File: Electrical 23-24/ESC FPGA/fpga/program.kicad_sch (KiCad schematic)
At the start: 7 parts, among them SW2 SW_Push, U1 XC6SLX4-TQG144

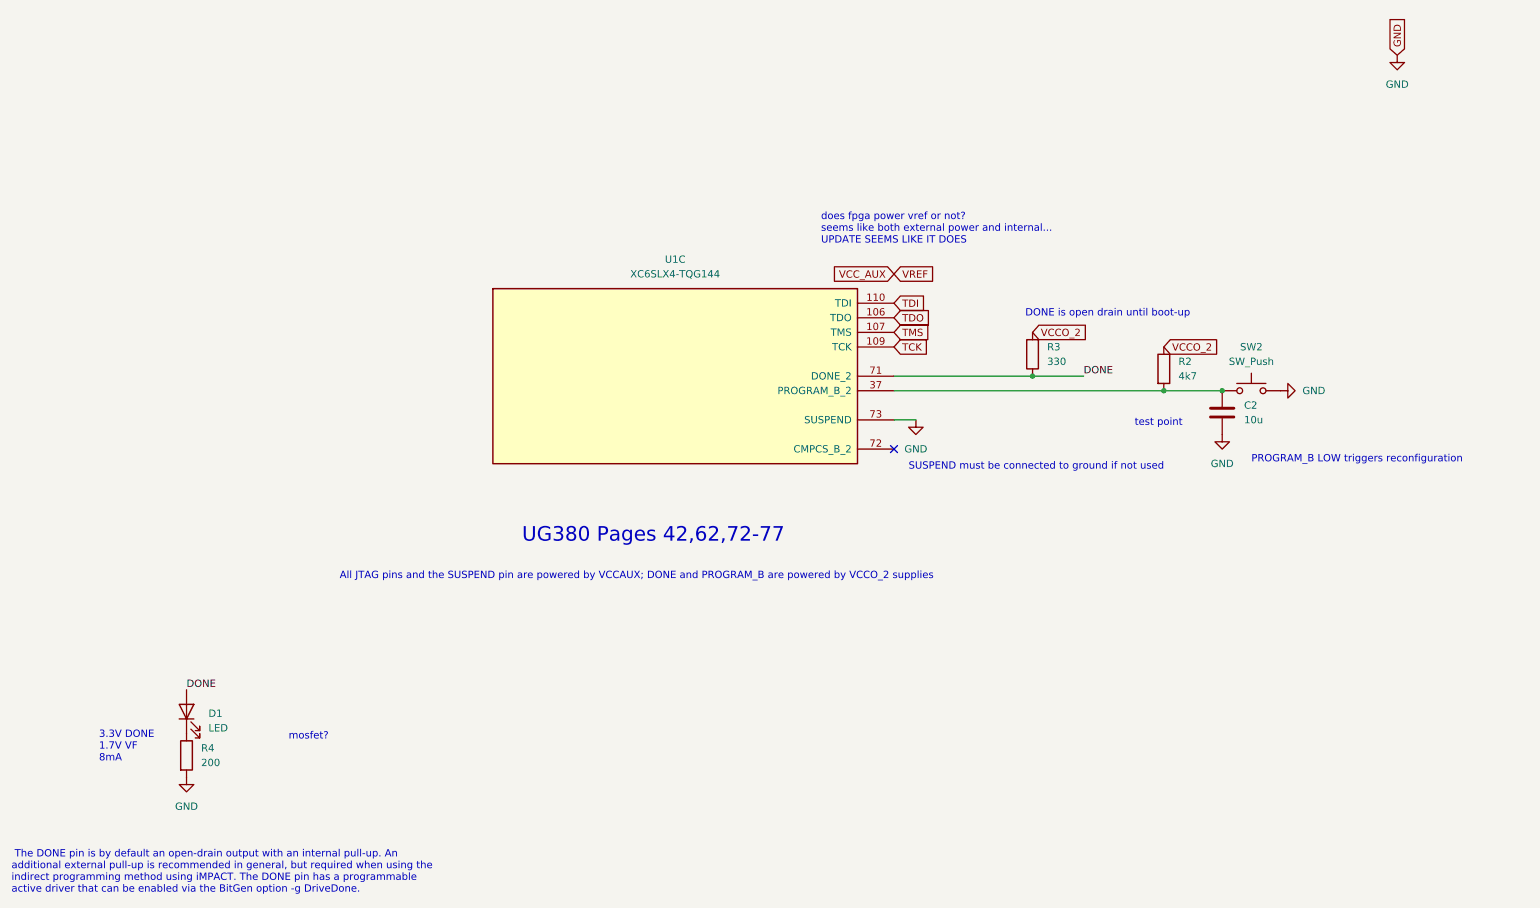
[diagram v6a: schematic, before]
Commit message: Made BOM, need to modify footprints
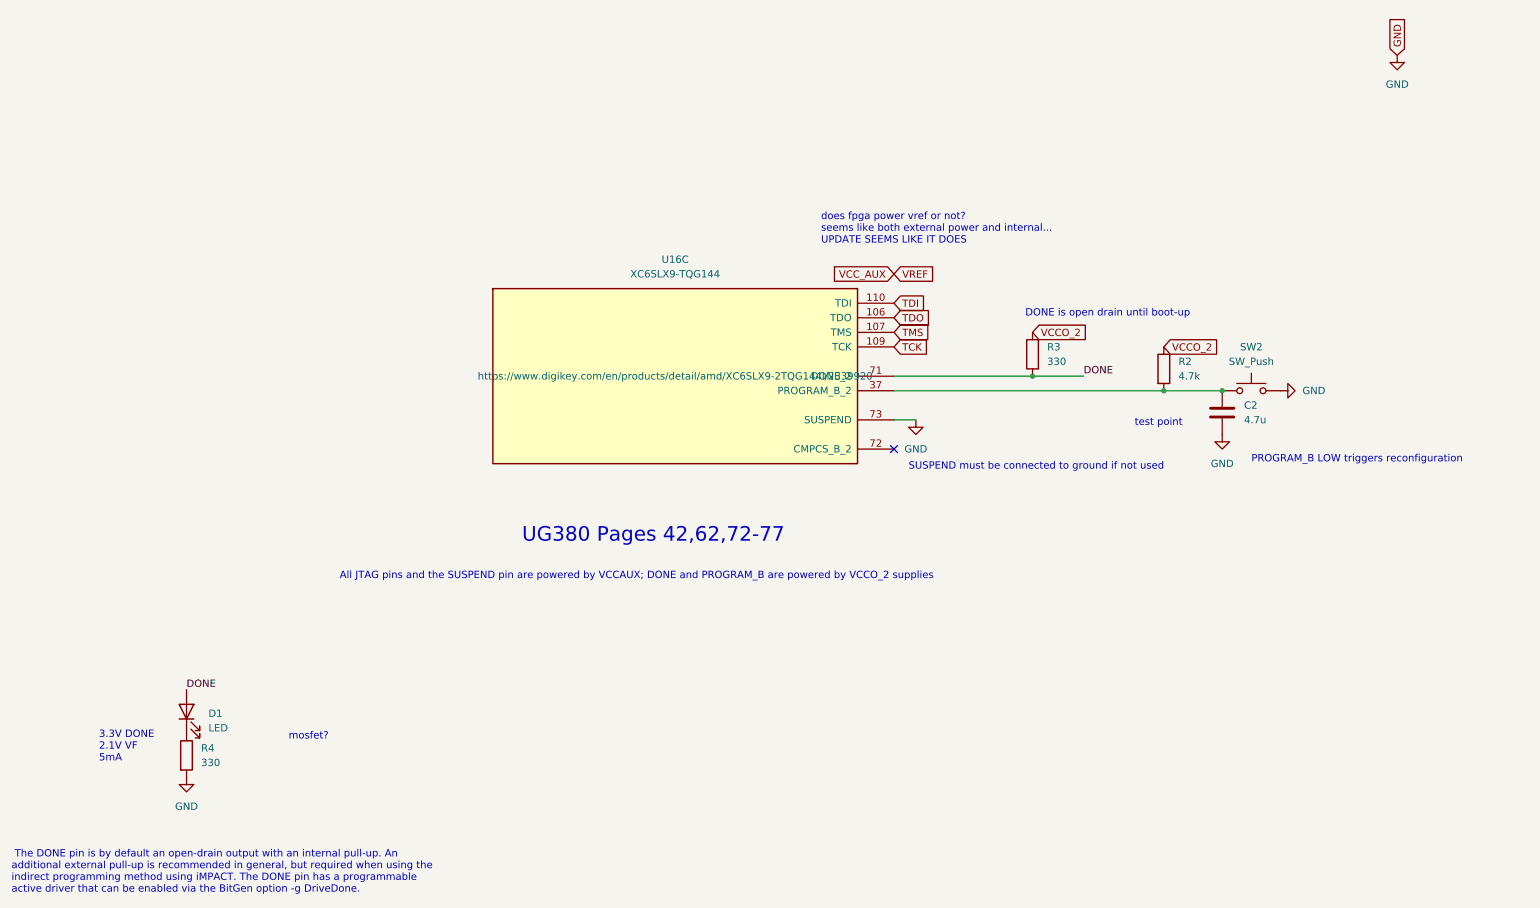
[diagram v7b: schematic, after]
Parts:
- removed U1: XC6SLX4-TQG144, symbol FPGA_Xilinx_Spartan6:XC6SLX4-TQG144
- added U16: XC6SLX9-TQG144, fpga:TQFP-144_20x20mm_P0.5mm, symbol FPGA_Xilinx_Spartan6:XC6SLX9-TQG144
- C2: value 10u -> 4.7u; footprint (none) -> Capacitor_SMD:C_0402_1005Metric_Pad0.74x0.62mm_HandSolder
- D1: footprint (none) -> LED_SMD:LED_0805_2012Metric_Pad1.15x1.40mm_HandSolder; Digi (none) -> https://www.digikey.com/en/products/detail/harvatek-corpora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
- R2: value 4k7 -> 4.7k; footprint (none) -> Resistor_SMD:R_0402_1005Metric_Pad0.72x0.64mm_HandSolder
- R3: footprint (none) -> Resistor_SMD:R_0402_1005Metric_Pad0.72x0.64mm_HandSolder
- R4: value 200 -> 330; footprint (none) -> Resistor_SMD:R_0402_1005Metric_Pad0.72x0.64mm_HandSolder
- SW2: footprint (none) -> fpga:NCA1; Digi (none) -> https://www.digikey.com/en/products/detail/cit-relay-and-sw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
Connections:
- net DONE: now also U16.71 (DONE_2)
- net GND: now also U16.73 (SUSPEND)
- net TCK: now also U16.109 (TCK)
- net TDI: now also U16.110 (TDI)
- net TDO: now also U16.106 (TDO)
- net TMS: now also U16.107 (TMS)
- net at C2.1, R2.2, SW2.1: now also U16.37 (PROGRAM_B_2)
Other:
- note added: "3.3V DONE 2.1V VF 5mA"
- note removed: "3.3V DONE 1.7V VF 8mA"
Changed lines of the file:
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@@
     (effects (font (size 1.27 1.27)) (justify left bottom))
   )
-  (text "3.3V DONE\n1.7V VF\n8mA" (at 40.64 157.48 0)
+  (text "3.3V DONE\n2.1V VF\n5mA" (at 40.64 157.48 0)
     (effects (font (size 1.27 1.27)) (justify left bottom))
   )
@@
       (effects (font (size 1.27 1.27)) (justify left))
     )
-    (property "Value" "10u" (at 240.03 97.79 0)
+    (property "Value" "4.7u" (at 240.03 97.79 0)
       (effects (font (size 1.27 1.27)) (justify left))
     )
-    (property "Footprint" "" (at 237.1852 100.33 0)
+    (property "Footprint" "Capacitor_SMD:C_0402_1005Metric_Pad0.74x0.62mm_HandSolder" (at 237.1852 100.33 0)
       (effects (font (size 1.27 1.27)) hide)
     )
@@
       (effects (font (size 1.27 1.27)) (justify left))
     )
-    (property "Value" "200" (at 58.42 157.48 0)
+    (property "Value" "330" (at 58.42 157.48 0)
       (effects (font (size 1.27 1.27)) (justify left))
     )
-    (property "Footprint" "" (at 54.102 156.21 90)
+    (property "Footprint" "Resistor_SMD:R_0402_1005Metric_Pad0.72x0.64mm_HandSolder" (at 54.102 156.21 90)
       (effects (font (size 1.27 1.27)) hide)
     )
@@
       (effects (font (size 1.27 1.27)))
     )
-    (property "Footprint" "" (at 241.3 87.63 0)
-      (effects (font (size 1.27 1.27)) hide)
-    )
-    (property "Datasheet" "~" (at 241.3 87.63 0)
+    (property "Footprint" "fpga:NCA1" (at 241.3 87.63 0)
+      (effects (font (size 1.27 1.27)) hide)
+    )
+    (property "Datasheet" "https://www.citrelay.com/Catalog%20Pages/SwitchCatalog/NC.pdf" (at 241.3 87.63 0)
+      (effects (font (size 1.27 1.27)) hide)
+    )
+    (property "Digi" "https://www.digikey.com/en/products/detail/cit-relay-and-switch/NCA1/12503265" (at 241.3 92.71 0)
       (effects (font (size 1.27 1.27)) hide)
     )
@@
         (path "/5bf59577-a814-4364-8f7a-37815cfb5474/5e885406-1c13-459a-ba1f-8e2447b7cb89"
           (reference "SW2") (unit 1)
+        )
+      )
+    )
+  )
+  (symbol (lib_id "Device:LED") (at 55.88 148.59 90) (unit 1)
+    (in_bom yes) (on_board yes) (dnp no) (fields_autoplaced)
+    (property "Reference" "D1" (at 59.69 148.9075 90)
+      (effects (font (size 1.27 1.27)) (justify right))
+    )
+    (property "Value" "LED" (at 59.69 151.4475 90)
+      (effects (font (size 1.27 1.27)) (justify right))
+    )
+    (property "Footprint" "LED_SMD:LED_0805_2012Metric_Pad1.15x1.40mm_HandSolder" (at 55.88 148.59 0)
+      (effects (font (size 1.27 1.27)) hide)
+    )
+    (property "Datasheet" "https://mm.digikey.com/Volume0/opasdata/d220001/medias/docus/3840/B1701UYG-20D000114U1930.pdf" (at 55.88 148.59 0)
+      (effects (font (size 1.27 1.27)) hide)
+    )
+    (property "Digi" "https://www.digikey.com/en/products/detail/harvatek-corporation/B1701UYG-20D000114U1930/16671747" (at 55.88 148.59 90)
+      (effects (font (size 1.27 1.27)) hide)
+    )
+    (pin "1")
+    (pin "2")
+    (instances
+      (project "fpga"
+        (path "/5bf59577-a814-4364-8f7a-37815cfb5474/5e885406-1c13-459a-ba1f-8e2447b7cb89"
+          (reference "D1") (unit 1)
+        )
+        (path "/5bf59577-a814-4364-8f7a-37815cfb5474/a7f1449c-b9d7-4bec-9483-b96d0a6d3b19"
+          (reference "D2") (unit 1)
         )
       )
@@
       (effects (font (size 1.27 1.27)) (justify right))
     )
-    (property "Footprint" "" (at 204.978 86.36 90)
+    (property "Footprint" "Resistor_SMD:R_0402_1005Metric_Pad0.72x0.64mm_HandSolder" (at 204.978 86.36 90)
       (effects (font (size 1.27 1.27)) hide)
     )
@@
     )
   )
-  (symbol (lib_id "Device:LED") (at 55.88 148.59 90) (unit 1)
-    (in_bom yes) (on_board yes) (dnp no) (fields_autoplaced)
-    (property "Reference" "D1" (at 59.69 148.9075 90)
-      (effects (font (size 1.27 1.27)) (justify right))
-    )
-    (property "Value" "LED" (at 59.69 151.4475 90)
-      (effects (font (size 1.27 1.27)) (justify right))
-    )
-    (property "Footprint" "" (at 55.88 148.59 0)
-      (effects (font (size 1.27 1.27)) hide)
-    )
-    (property "Datasheet" "~" (at 55.88 148.59 0)
-      (effects (font (size 1.27 1.27)) hide)
-    )
-    (pin "1")
-    (pin "2")
-    (instances
-      (project "fpga"
-        (path "/5bf59577-a814-4364-8f7a-37815cfb5474/5e885406-1c13-459a-ba1f-8e2447b7cb89"
-          (reference "D1") (unit 1)
-        )
-      )
-    )
-  )
-  (symbol (lib_id "Device:R") (at 226.06 88.9 0) (unit 1)
-    (in_bom yes) (on_board yes) (dnp no) (fields_autoplaced)
-    (property "Reference" "R2" (at 228.6 87.63 0)
-      (effects (font (size 1.27 1.27)) (justify left))
-    )
-    (property "Value" "4k7" (at 228.6 90.17 0)
-      (effects (font (size 1.27 1.27)) (justify left))
-    )
-    (property "Footprint" "" (at 224.282 88.9 90)
-      (effects (font (size 1.27 1.27)) hide)
-    )
-    (property "Datasheet" "~" (at 226.06 88.9 0)
-      (effects (font (size 1.27 1.27)) hide)
-    )
-    (pin "1")
-    (pin "2")
-    (instances
-      (project "fpga"
-        (path "/5bf59577-a814-4364-8f7a-37815cfb5474/5e885406-1c13-459a-ba1f-8e2447b7cb89"
-          (reference "R2") (unit 1)
-        )
-      )
-    )
-  )
-  (symbol (lib_id "power:GND") (at 236.22 100.33 0) (unit 1)
-    (in_bom yes) (on_board yes) (dnp no) (fields_autoplaced)
-    (property "Reference" "#PWR05" (at 236.22 106.68 0)
-      (effects (font (size 1.27 1.27)) hide)
-    )
-    (property "Value" "GND" (at 236.22 105.41 0)
-      (effects (font (size 1.27 1.27)))
-    )
-    (property "Footprint" "" (at 236.22 100.33 0)
-      (effects (font (size 1.27 1.27)) hide)
-    )
-    (property "Datasheet" "" (at 236.22 100.33 0)
-      (effects (font (size 1.27 1.27)) hide)
-    )
-    (pin "1")
-    (instances
-      (project "fpga"
-        (path "/5bf59577-a814-4364-8f7a-37815cfb5474/5e885406-1c13-459a-ba1f-8e2447b7cb89"
-          (reference "#PWR05") (unit 1)
-        )
-      )
-    )
-  )
-  (symbol (lib_id "FPGA_Xilinx_Spartan6:XC6SLX4-TQG144") (at 140.97 90.17 0) (unit 3)
-    (in_bom yes) (on_board yes) (dnp no) (fields_autoplaced)
-    (property "Reference" "U1" (at 140.97 69.85 0)
-      (effects (font (size 1.27 1.27)))
-    )
-    (property "Value" "XC6SLX4-TQG144" (at 140.97 72.39 0)
-      (effects (font (size 1.27 1.27)))
-    )
-    (property "Footprint" "" (at 140.97 90.17 0)
-      (effects (font (size 1.27 1.27)) hide)
-    )
-    (property "Datasheet" "" (at 140.97 90.17 0)
+  (symbol (lib_id "FPGA_Xilinx_Spartan6:XC6SLX9-TQG144") (at 140.97 90.17 0) (unit 3)
+    (in_bom yes) (on_board yes) (dnp no) (fields_autoplaced)
+    (property "Reference" "U16" (at 140.97 69.85 0)
+      (effects (font (size 1.27 1.27)))
+    )
+    (property "Value" "XC6SLX9-TQG144" (at 140.97 72.39 0)
+      (effects (font (size 1.27 1.27)))
+    )
+    (property "Footprint" "fpga:TQFP-144_20x20mm_P0.5mm" (at 140.97 90.17 0)
+      (effects (font (size 1.27 1.27)) hide)
+    )
+    (property "Datasheet" "https://www.digikey.com/en/products/detail/amd/XC6SLX9-2TQG144I/2339920" (at 140.97 90.17 0)
       (effects (font (size 1.27 1.27)))
     )
@@
       (project "fpga"
         (path "/5bf59577-a814-4364-8f7a-37815cfb5474/1f83b38b-56ef-4110-879b-13379f9dd920"
+          (reference "U16") (unit 3)
+        )
+        (path "/5bf59577-a814-4364-8f7a-37815cfb5474/a286b274-4434-47ab-983d-e64806fdcbd6"
           (reference "U1") (unit 3)
         )
-        (path "/5bf59577-a814-4364-8f7a-37815cfb5474/a286b274-4434-47ab-983d-e64806fdcbd6"
-          (reference "U2") (unit 3)
-        )
-        (path "/5bf59577-a814-4364-8f7a-37815cfb5474/5e885406-1c13-459a-ba1f-8e2447b7cb89"
-          (reference "U3") (unit 3)
-        )
-        (path "/5bf59577-a814-4364-8f7a-37815cfb5474/3e04db34-3f8a-4742-be82-6fa24c009343"
-          (reference "U4") (unit 3)
-        )
-      )
+        (path "/5bf59577-a814-4364-8f7a-37815cfb5474/5e885406-1c13-459a-ba1f-8e2447b7cb89"
+          (reference "U1") (unit 3)
+        )
+      )
+    )
+  )
+  (symbol (lib_id "Device:R") (at 226.06 88.9 0) (unit 1)
+    (in_bom yes) (on_board yes) (dnp no) (fields_autoplaced)
+    (property "Reference" "R2" (at 228.6 87.63 0)
+      (effects (font (size 1.27 1.27)) (justify left))
+    )
+    (property "Value" "4.7k" (at 228.6 90.17 0)
+      (effects (font (size 1.27 1.27)) (justify left))
+    )
+    (property "Footprint" "Resistor_SMD:R_0402_1005Metric_Pad0.72x0.64mm_HandSolder" (at 224.282 88.9 90)
+      (effects (font (size 1.27 1.27)) hide)
+    )
+    (property "Datasheet" "~" (at 226.06 88.9 0)
+      (effects (font (size 1.27 1.27)) hide)
+    )
+    (pin "1")
+    (pin "2")
+    (instances
+      (project "fpga"
+        (path "/5bf59577-a814-4364-8f7a-37815cfb5474/5e885406-1c13-459a-ba1f-8e2447b7cb89"
+          (reference "R2") (unit 1)
+        )
+      )
+    )
+  )
+  (symbol (lib_id "power:GND") (at 236.22 100.33 0) (unit 1)
+    (in_bom yes) (on_board yes) (dnp no) (fields_autoplaced)
+    (property "Reference" "#PWR05" (at 236.22 106.68 0)
+      (effects (font (size 1.27 1.27)) hide)
+    )
+    (property "Value" "GND" (at 236.22 105.41 0)
+      (effects (font (size 1.27 1.27)))
+    )
+    (property "Footprint" "" (at 236.22 100.33 0)
+      (effects (font (size 1.27 1.27)) hide)
+    )
+    (property "Datasheet" "" (at 236.22 100.33 0)
+      (effects (font (size 1.27 1.27)) hide)
+    )
+    (pin "1")
+    (instances
+      (project "fpga"
+        (path "/5bf59577-a814-4364-8f7a-37815cfb5474/5e885406-1c13-459a-ba1f-8e2447b7cb89"
+          (reference "#PWR05") (unit 1)
+        )
+      )

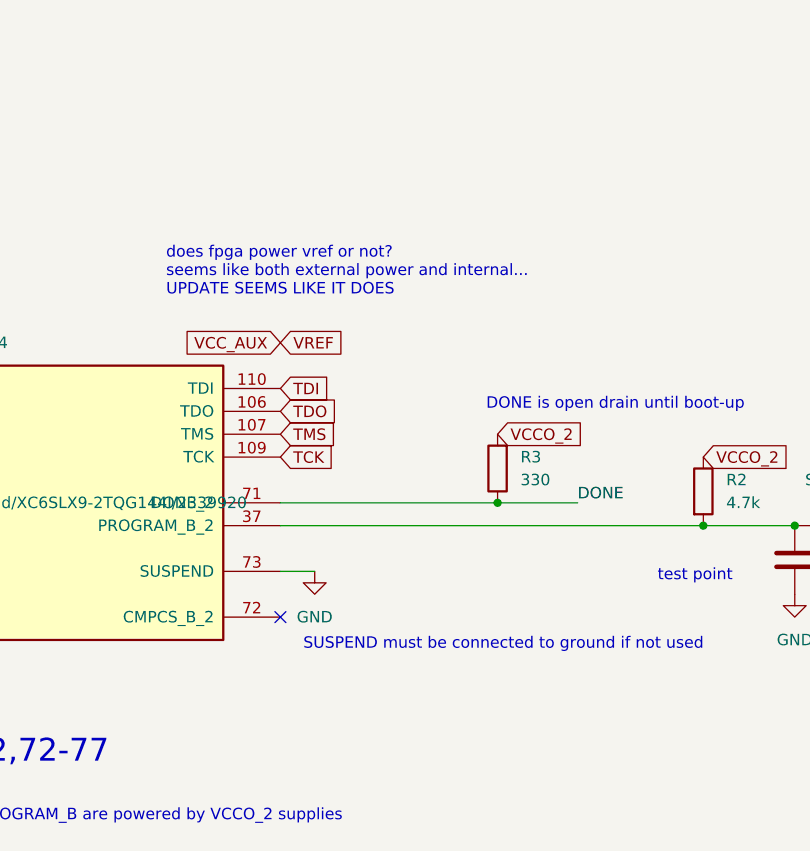
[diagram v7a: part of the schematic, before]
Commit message: Finish groupings on FPGA PCB
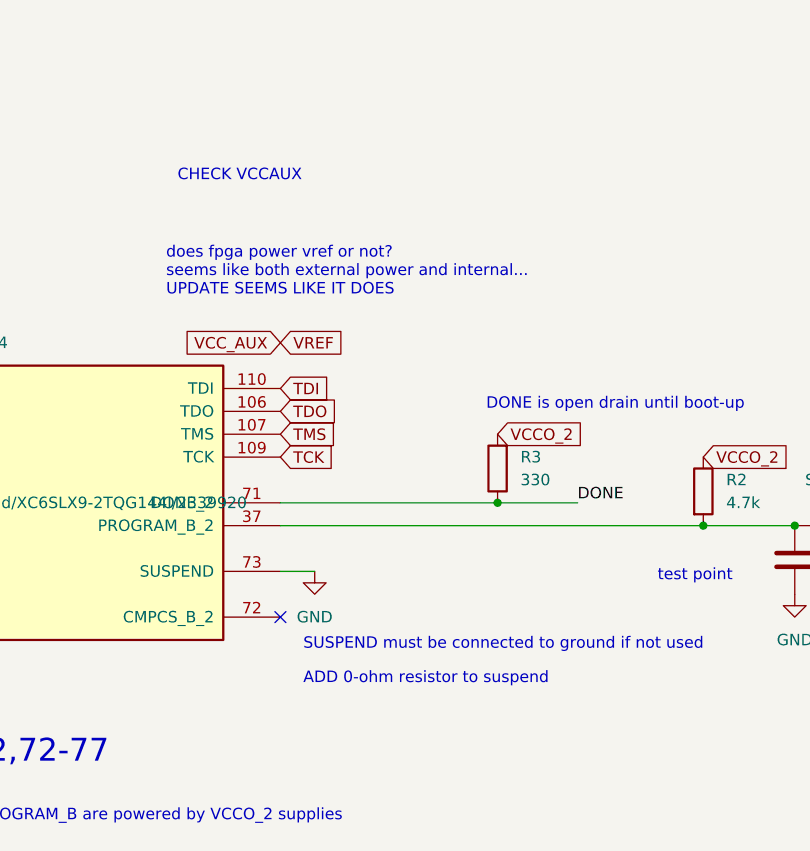
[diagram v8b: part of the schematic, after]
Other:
- note added: "ADD 0-ohm resistor to suspend"
- note added: "CHECK VCCAUX"
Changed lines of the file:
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@@
+    (effects (font (size 1.27 1.27)) (justify left bottom))
+  )
+  (text "CHECK VCCAUX" (at 167.64 54.61 0)
     (effects (font (size 1.27 1.27)) (justify left bottom))
   )
@@
     (effects (font (size 1.27 1.27)) (justify left bottom))
   )
+  (text "ADD 0-ohm resistor to suspend" (at 181.61 110.49 0)
+    (effects (font (size 1.27 1.27)) (justify left bottom))
+  )
